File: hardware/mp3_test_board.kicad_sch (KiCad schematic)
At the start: 0 parts

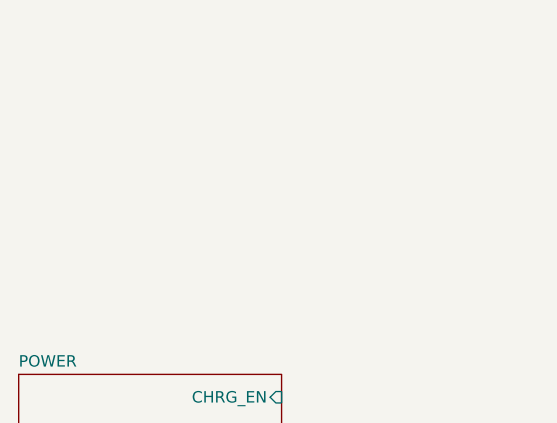
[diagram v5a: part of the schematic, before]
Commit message: added new power list
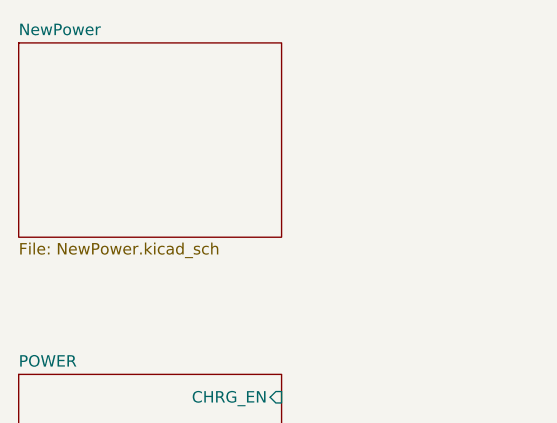
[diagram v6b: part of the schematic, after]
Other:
- added sheet NewPower (NewPower.kicad_sch)
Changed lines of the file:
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@@
     (stroke (width 0) (type default) (color 0 0 0 0))
+  )
+  (sheet (at 62.23 33.02) (size 29.21 21.59) (fields_autoplaced)
+    (stroke (width 0.1524) (type solid) (color 0 0 0 0))
+    (fill (color 0 0 0 0.0000))
+    (property "Sheet name" "NewPower" (id 0) (at 62.23 32.3084 0)
+      (effects (font (size 1.27 1.27)) (justify left bottom))
+    )
+    (property "Sheet file" "NewPower.kicad_sch" (id 1) (at 62.23 55.1946 0)
+      (effects (font (size 1.27 1.27)) (justify left top))
+    )
   )
   (sheet (at 123.19 69.85) (size 36.83 26.67)
@@
     (path "/e1791f45-9313-4623-bca3-b0a68fdadfbe" (page "2"))
     (path "/494fd4b1-1de7-49fe-827f-914491efe850" (page "4"))
+    (path "/3ea3f31d-a82c-4aa5-88e5-12314efba5ef" (page "5"))
     (path "/8a184ff4-f009-4368-ae0f-59dfbdc06c07" (page "5"))
   )
@@
       (reference "#PWR0211") (unit 1) (value "GND") (footprint "")
     )
+    (path "/3ea3f31d-a82c-4aa5-88e5-12314efba5ef/06182965-4826-4d31-ab4d-49594a517f88"
+      (reference "#PWR?") (unit 1) (value "VCC") (footprint "")
+    )
+    (path "/3ea3f31d-a82c-4aa5-88e5-12314efba5ef/0bce128f-c153-4d96-b11e-8f1c5d9ffb11"
+      (reference "#PWR?") (unit 1) (value "+3V3") (footprint "")
+    )
+    (path "/3ea3f31d-a82c-4aa5-88e5-12314efba5ef/11b0f9a9-c0cc-420b-9056-c4c57a2cd8ae"
+      (reference "#PWR?") (unit 1) (value "VCC") (footprint "")
+    )
+    (path "/3ea3f31d-a82c-4aa5-88e5-12314efba5ef/14f8af96-2a38-4df8-a6c0-b4f7bba1c15b"
+      (reference "#PWR?") (unit 1) (value "GND") (footprint "")
+    )
+    (path "/3ea3f31d-a82c-4aa5-88e5-12314efba5ef/168daa6b-3a2e-4a3d-9882-9d2b5cde4f31"
+      (reference "#PWR?") (unit 1) (value "GND") (footprint "")
+    )
+    (path "/3ea3f31d-a82c-4aa5-88e5-12314efba5ef/2bfe1cd3-98d7-4e50-96fe-226ce7a48a03"
+      (reference "#PWR?") (unit 1) (value "GND") (footprint "")
+    )
+    (path "/3ea3f31d-a82c-4aa5-88e5-12314efba5ef/32ff7333-6a06-416a-84b1-c8e6c8587922"
+      (reference "#PWR?") (unit 1) (value "+2V5") (footprint "")
+    )
+    (path "/3ea3f31d-a82c-4aa5-88e5-12314efba5ef/474ba75b-3a60-4d1a-bb1c-6a481217af80"
+      (reference "#PWR?") (unit 1) (value "GND") (footprint "")
+    )
+    (path "/3ea3f31d-a82c-4aa5-88e5-12314efba5ef/477799b4-5747-4db9-af5a-97132ae9cbb5"
+      (reference "#PWR?") (unit 1) (value "GND") (footprint "")
+    )
+    (path "/3ea3f31d-a82c-4aa5-88e5-12314efba5ef/4b311a8a-6d20-4c67-861b-da025d54be42"
+      (reference "#PWR?") (unit 1) (value "GND") (footprint "")
+    )
+    (path "/3ea3f31d-a82c-4aa5-88e5-12314efba5ef/4eb77dbc-20bc-4b93-b2dc-e89ff4947d29"
+      (reference "#PWR?") (unit 1) (value "GND") (footprint "")
+    )
+    (path "/3ea3f31d-a82c-4aa5-88e5-12314efba5ef/5fb3bffc-e9c6-4cff-af72-73faefa1ab9c"
+      (reference "#PWR?") (unit 1) (value "VCC") (footprint "")
+    )
+    (path "/3ea3f31d-a82c-4aa5-88e5-12314efba5ef/8dd72828-3d91-4eab-9d65-c7da47bf9865"
+      (reference "#PWR?") (unit 1) (value "+1V1") (footprint "")
+    )
+    (path "/3ea3f31d-a82c-4aa5-88e5-12314efba5ef/90e42987-3f1d-41df-990d-075f0a2f6fbc"
+      (reference "#PWR?") (unit 1) (value "+1V1") (footprint "")
+    )
+    (path "/3ea3f31d-a82c-4aa5-88e5-12314efba5ef/91f41863-bb16-4ee5-87a1-f0b14cc92a99"
+      (reference "#PWR?") (unit 1) (value "GND") (footprint "")
+    )
+    (path "/3ea3f31d-a82c-4aa5-88e5-12314efba5ef/977a2139-f80b-4a88-8bf9-1dcce1dccea0"
+      (reference "#PWR?") (unit 1) (value "GND") (footprint "")
+    )
+    (path "/3ea3f31d-a82c-4aa5-88e5-12314efba5ef/a4663c17-4430-4e13-923d-0e9396d2b4e2"
+      (reference "#PWR?") (unit 1) (value "GND") (footprint "")
+    )
+    (path "/3ea3f31d-a82c-4aa5-88e5-12314efba5ef/a4de41be-e5ff-4ff9-815f-671c4a01d4e2"
+      (reference "#PWR?") (unit 1) (value "VCC") (footprint "")
+    )
+    (path "/3ea3f31d-a82c-4aa5-88e5-12314efba5ef/a5a16e5f-bf3b-4b93-9d78-cc14b1499b59"
+      (reference "#PWR?") (unit 1) (value "+3V0") (footprint "")
+    )
+    (path "/3ea3f31d-a82c-4aa5-88e5-12314efba5ef/b5115803-c757-4c8b-a7b1-d4fd26ba3464"
+      (reference "#PWR?") (unit 1) (value "GND") (footprint "")
+    )
+    (path "/3ea3f31d-a82c-4aa5-88e5-12314efba5ef/d46c1fda-53a7-41e7-a9a0-039fe17726ad"
+      (reference "#PWR?") (unit 1) (value "GND") (footprint "")
+    )
+    (path "/3ea3f31d-a82c-4aa5-88e5-12314efba5ef/f11ab8d7-ad9f-4d7c-898d-0720f5f8f396"
+      (reference "#PWR?") (unit 1) (value "VCC") (footprint "")
+    )
     (path "/e1791f45-9313-4623-bca3-b0a68fdadfbe/ee67da40-1ebe-4920-a137-523a8361865b"
       (reference "C1") (unit 1) (value "C") (footprint "rlib_passive:C_0603_1608Metric")
@@
       (reference "C111") (unit 1) (value "0.1u") (footprint "rlib_passive:C_0603_1608Metric")
     )
+    (path "/3ea3f31d-a82c-4aa5-88e5-12314efba5ef/4a52cd56-ae45-4066-870d-e45e5273b532"
+      (reference "C?") (unit 1) (value "C") (footprint "")
+    )
+    (path "/3ea3f31d-a82c-4aa5-88e5-12314efba5ef/68b8dbbc-863a-4be4-8ed8-d80afc46fd58"
+      (reference "C?") (unit 1) (value "C") (footprint "")
+    )
+    (path "/3ea3f31d-a82c-4aa5-88e5-12314efba5ef/76ea2f8f-0486-436c-9c0e-27d1d16aa96c"
+      (reference "C?") (unit 1) (value "C") (footprint "")
+    )
+    (path "/3ea3f31d-a82c-4aa5-88e5-12314efba5ef/838dd06e-943c-4c6f-8b8a-9a9ac960a029"
+      (reference "C?") (unit 1) (value "C") (footprint "")
+    )
+    (path "/3ea3f31d-a82c-4aa5-88e5-12314efba5ef/8a000461-9663-49f7-b7a0-83ba032b5561"
+      (reference "C?") (unit 1) (value "C") (footprint "")
+    )
+    (path "/3ea3f31d-a82c-4aa5-88e5-12314efba5ef/8f43fe18-96d0-4c57-85e5-fc7b8eff660f"
+      (reference "C?") (unit 1) (value "C") (footprint "")
+    )
+    (path "/3ea3f31d-a82c-4aa5-88e5-12314efba5ef/a3ed2766-277f-4729-af5c-dcb3988bd75b"
+      (reference "C?") (unit 1) (value "C") (footprint "")
+    )
+    (path "/3ea3f31d-a82c-4aa5-88e5-12314efba5ef/c12e8438-50c9-4bc3-9db4-f9c3f34d235a"
+      (reference "C?") (unit 1) (value "C") (footprint "")
+    )
+    (path "/3ea3f31d-a82c-4aa5-88e5-12314efba5ef/e00ee5b2-0209-4e77-a5cd-5beb7749f76c"
+      (reference "C?") (unit 1) (value "C") (footprint "")
+    )
+    (path "/3ea3f31d-a82c-4aa5-88e5-12314efba5ef/e43a8bfa-de41-48b9-8949-b15e79ae98c6"
+      (reference "C?") (unit 1) (value "C") (footprint "")
+    )
+    (path "/3ea3f31d-a82c-4aa5-88e5-12314efba5ef/f834eab8-4b44-4f47-bc71-f021b2e3678c"
+      (reference "C?") (unit 1) (value "C") (footprint "")
+    )
     (path "/e1791f45-9313-4623-bca3-b0a68fdadfbe/d6244fd8-714f-4102-a06e-12a381d507e1"
       (reference "D1") (unit 1) (value "PESD3V3L1BA") (footprint "rlib_passive:D_SOD-323F")
@@
       (reference "L9") (unit 1) (value "L") (footprint "")
     )
+    (path "/3ea3f31d-a82c-4aa5-88e5-12314efba5ef/1e210081-84ac-49b8-a218-8c1b362762c0"
+      (reference "L?") (unit 1) (value "L") (footprint "")
+    )
+    (path "/3ea3f31d-a82c-4aa5-88e5-12314efba5ef/59164df0-164b-4f11-b3b8-3050bb023263"
+      (reference "L?") (unit 1) (value "L") (footprint "")
+    )
+    (path "/3ea3f31d-a82c-4aa5-88e5-12314efba5ef/5e1663c5-a5d1-41c5-9d7f-c5ef1a2e1e1e"
+      (reference "L?") (unit 1) (value "L") (footprint "")
+    )
+    (path "/3ea3f31d-a82c-4aa5-88e5-12314efba5ef/c8e5629a-938d-44f5-939c-779c3c1fc5e1"
+      (reference "L?") (unit 1) (value "L") (footprint "")
+    )
+    (path "/3ea3f31d-a82c-4aa5-88e5-12314efba5ef/d0bbf29b-38c2-4ab6-9360-1d831c2ebc69"
+      (reference "L?") (unit 1) (value "L") (footprint "")
+    )
     (path "/e1791f45-9313-4623-bca3-b0a68fdadfbe/c7d10f1d-e909-40e0-8ea5-2588fa01f48d"
       (reference "NT1") (unit 1) (value "NetTie_2") (footprint "")
@@
       (reference "R67") (unit 1) (value "220") (footprint "")
     )
+    (path "/3ea3f31d-a82c-4aa5-88e5-12314efba5ef/7cefdcc4-8ec1-40ae-9db9-7f927fd5a27b"
+      (reference "R?") (unit 1) (value "R") (footprint "")
+    )
+    (path "/3ea3f31d-a82c-4aa5-88e5-12314efba5ef/ded9971f-0461-4b20-a25a-7a74c3abd775"
+      (reference "R?") (unit 1) (value "R") (footprint "")
+    )
     (path "/e1791f45-9313-4623-bca3-b0a68fdadfbe/34008909-d15a-432e-8a83-89239de5595a"
       (reference "SW1") (unit 1) (value "TS-1010-C-A") (footprint "rlib_buttons:GT-TC054A-H035-L1")
@@
       (reference "U15") (unit 3) (value "OPA1656") (footprint "rlib_ic:SOIC-8_3.9x4.9mm_P1.27mm")
     )
+    (path "/3ea3f31d-a82c-4aa5-88e5-12314efba5ef/f83f8e92-699a-4252-b6dc-9fcc839c7fb5"
+      (reference "U?") (unit 1) (value "RK816") (footprint "")
+    )
     (path "/494fd4b1-1de7-49fe-827f-914491efe850/064e1b76-24d1-4254-9708-33fdba07e7fa"

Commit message: some changes
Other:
- removed sheet POWER
- added sheet NewPower2 (NewPower2.kicad_sch)
